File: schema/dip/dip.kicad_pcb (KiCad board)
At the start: 2 copper layers, 40.2 x 20.2 mm, 5 parts, among them J1 Conn_01x04_Male, J2 Conn_01x04_Male, SW1 SW_DIP_x04

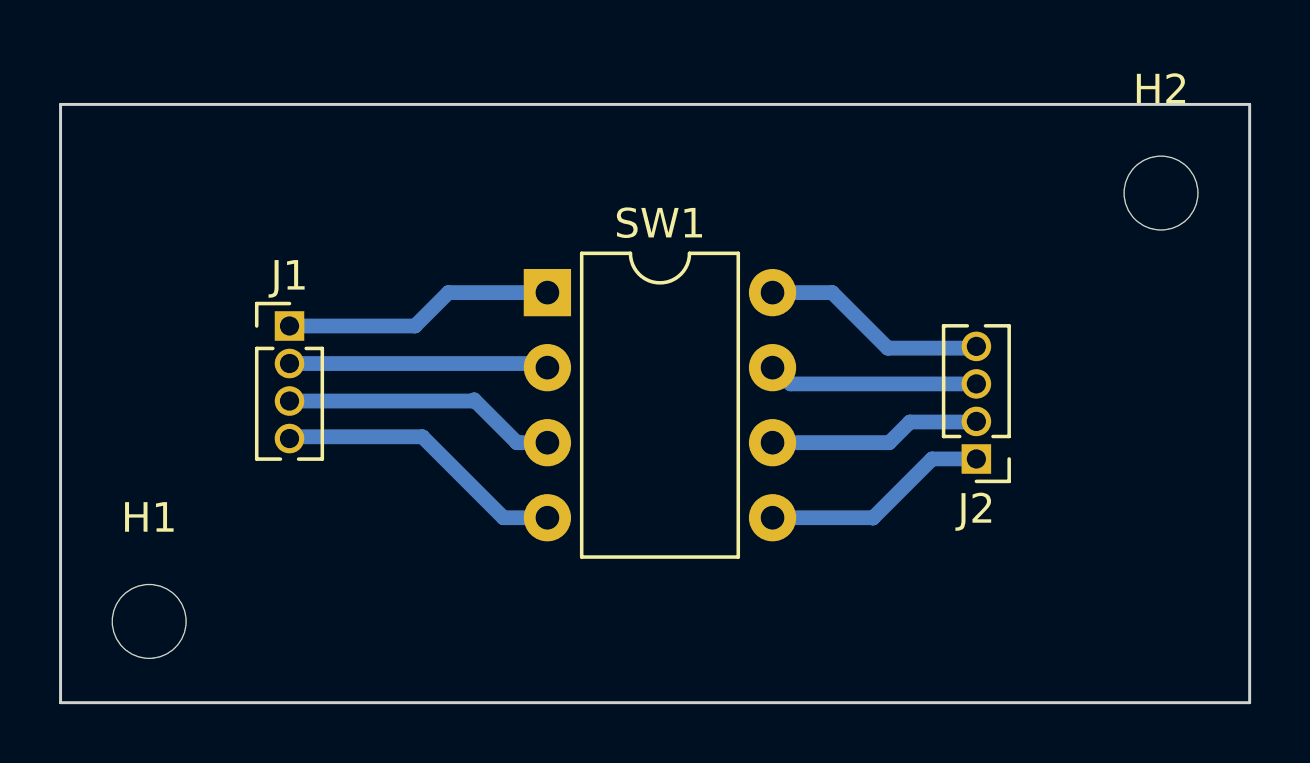
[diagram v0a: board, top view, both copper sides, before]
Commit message: support 02-silk directory
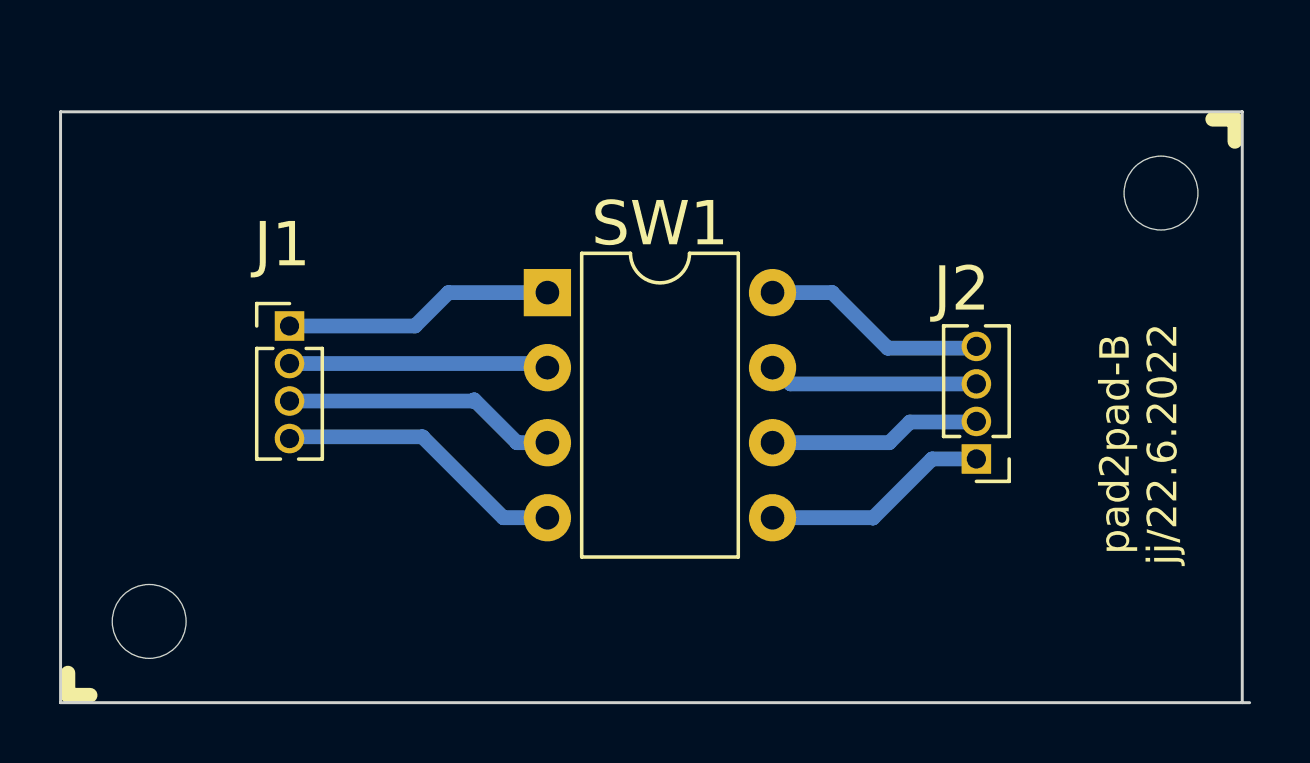
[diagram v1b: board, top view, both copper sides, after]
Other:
- board size 40.2 x 20.2 mm -> 40.2 x 20 mm
- board text added: "pad2pad-B jj/22.6.2022"

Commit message: alignment edges fixed
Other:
- board size 40.2 x 20 mm -> 40 x 20 mm

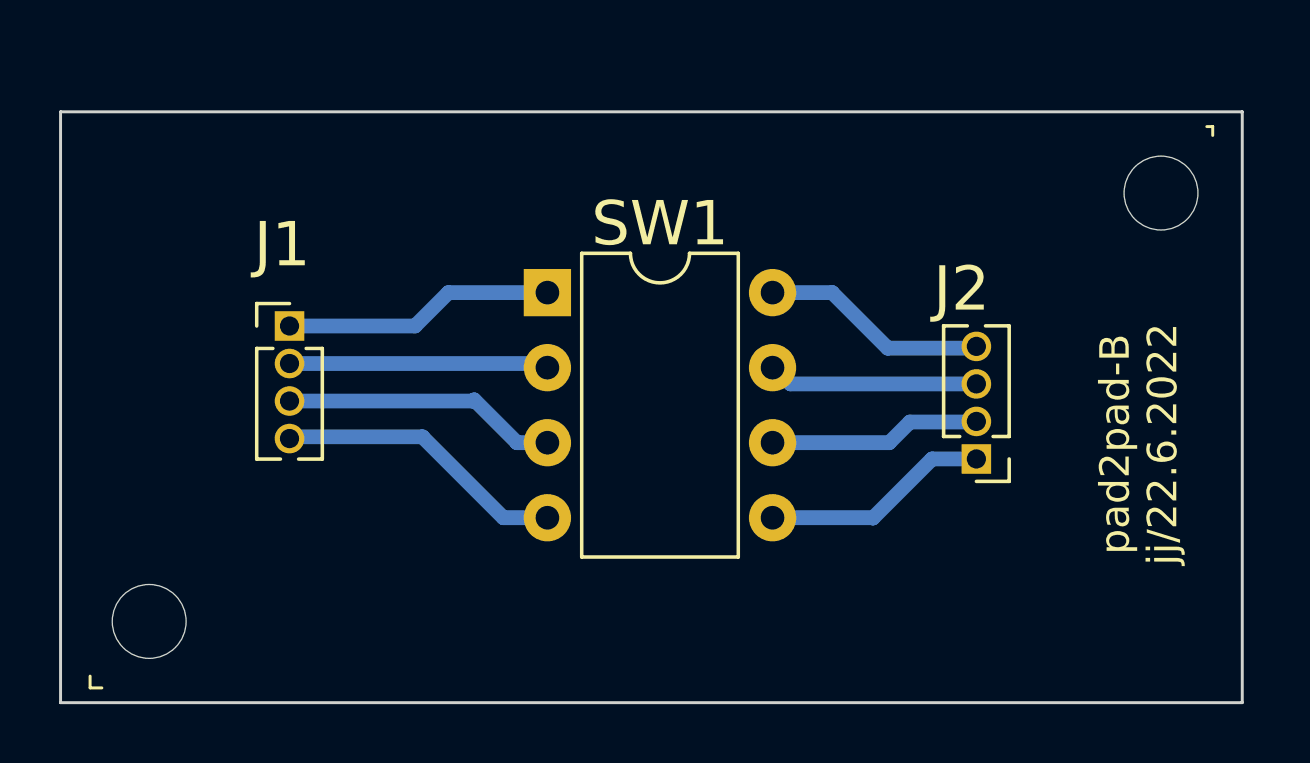
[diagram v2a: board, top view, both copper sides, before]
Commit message: fixed example: pad2pad, dip, added: milldrill option
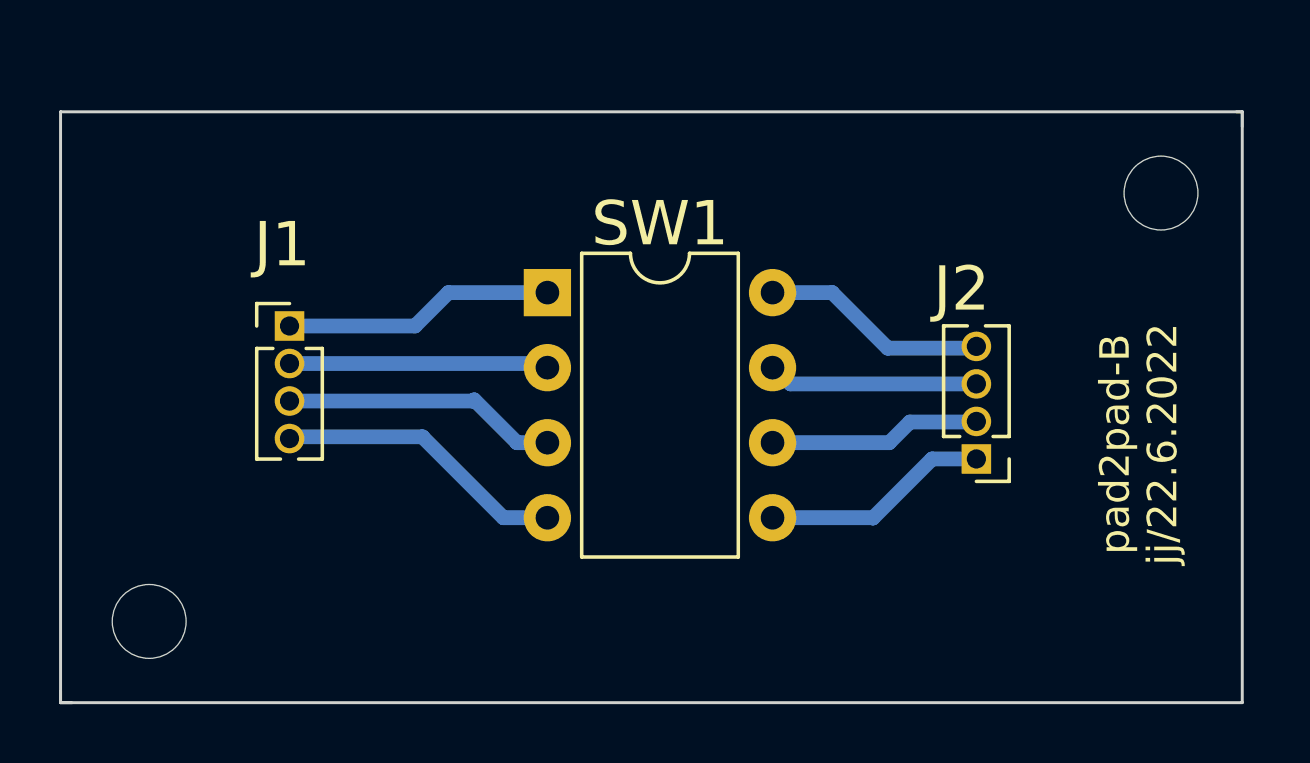
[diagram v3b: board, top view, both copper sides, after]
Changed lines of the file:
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@@
       (effects (font (size 1 1) (thickness 0.15)))
     )
+    (fp_circle (center 0 0) (end 2.5 0) (layer Cmts.User) (width 0.15))
     (fp_circle (center 0 0) (end 2.75 0) (layer F.CrtYd) (width 0.05))
-    (fp_circle (center 0 0) (end 2.5 0) (layer Cmts.User) (width 0.15))
     (fp_text user %R (at 0.3 0) (layer F.Fab)
       (effects (font (size 1 1) (thickness 0.15)))
@@
       (effects (font (size 1 1) (thickness 0.15)))
     )
+    (fp_circle (center 0 0) (end 2.5 0) (layer Cmts.User) (width 0.15))
     (fp_circle (center 0 0) (end 2.75 0) (layer F.CrtYd) (width 0.05))
-    (fp_circle (center 0 0) (end 2.5 0) (layer Cmts.User) (width 0.15))
     (fp_text user %R (at 0.3 0) (layer F.Fab)
       (effects (font (size 1 1) (thickness 0.15)))
@@
       (effects (font (size 1 1) (thickness 0.15)))
     )
+    (fp_line (start 1.635 -1.27) (end 6.985 -1.27) (layer F.Fab) (width 0.1))
+    (fp_line (start 6.985 -1.27) (end 6.985 8.89) (layer F.Fab) (width 0.1))
+    (fp_line (start 6.985 8.89) (end 0.635 8.89) (layer F.Fab) (width 0.1))
+    (fp_line (start 0.635 8.89) (end 0.635 -0.27) (layer F.Fab) (width 0.1))
+    (fp_line (start 0.635 -0.27) (end 1.635 -1.27) (layer F.Fab) (width 0.1))
+    (fp_line (start 2.81 -1.33) (end 1.16 -1.33) (layer F.SilkS) (width 0.12))
+    (fp_line (start 1.16 -1.33) (end 1.16 8.95) (layer F.SilkS) (width 0.12))
+    (fp_line (start 1.16 8.95) (end 6.46 8.95) (layer F.SilkS) (width 0.12))
+    (fp_line (start 6.46 8.95) (end 6.46 -1.33) (layer F.SilkS) (width 0.12))
+    (fp_line (start 6.46 -1.33) (end 4.81 -1.33) (layer F.SilkS) (width 0.12))
+    (fp_line (start -1.1 -1.55) (end -1.1 9.15) (layer F.CrtYd) (width 0.05))
+    (fp_line (start -1.1 9.15) (end 8.7 9.15) (layer F.CrtYd) (width 0.05))
+    (fp_line (start 8.7 9.15) (end 8.7 -1.55) (layer F.CrtYd) (width 0.05))
     (fp_line (start 8.7 -1.55) (end -1.1 -1.55) (layer F.CrtYd) (width 0.05))
-    (fp_line (start 8.7 9.15) (end 8.7 -1.55) (layer F.CrtYd) (width 0.05))
-    (fp_line (start -1.1 9.15) (end 8.7 9.15) (layer F.CrtYd) (width 0.05))
-    (fp_line (start -1.1 -1.55) (end -1.1 9.15) (layer F.CrtYd) (width 0.05))
-    (fp_line (start 6.46 -1.33) (end 4.81 -1.33) (layer F.SilkS) (width 0.12))
-    (fp_line (start 6.46 8.95) (end 6.46 -1.33) (layer F.SilkS) (width 0.12))
-    (fp_line (start 1.16 8.95) (end 6.46 8.95) (layer F.SilkS) (width 0.12))
-    (fp_line (start 1.16 -1.33) (end 1.16 8.95) (layer F.SilkS) (width 0.12))
-    (fp_line (start 2.81 -1.33) (end 1.16 -1.33) (layer F.SilkS) (width 0.12))
-    (fp_line (start 0.635 -0.27) (end 1.635 -1.27) (layer F.Fab) (width 0.1))
-    (fp_line (start 0.635 8.89) (end 0.635 -0.27) (layer F.Fab) (width 0.1))
-    (fp_line (start 6.985 8.89) (end 0.635 8.89) (layer F.Fab) (width 0.1))
-    (fp_line (start 6.985 -1.27) (end 6.985 8.89) (layer F.Fab) (width 0.1))
-    (fp_line (start 1.635 -1.27) (end 6.985 -1.27) (layer F.Fab) (width 0.1))
     (fp_text user %R (at 3.81 3.81) (layer F.Fab)
       (effects (font (size 1 1) (thickness 0.15)))
@@
       (effects (font (size 1 1) (thickness 0.15)))
     )
+    (fp_line (start -0.525 -0.635) (end 1.05 -0.635) (layer F.Fab) (width 0.1))
+    (fp_line (start 1.05 -0.635) (end 1.05 4.445) (layer F.Fab) (width 0.1))
+    (fp_line (start 1.05 4.445) (end -1.05 4.445) (layer F.Fab) (width 0.1))
+    (fp_line (start -1.05 4.445) (end -1.05 -0.11) (layer F.Fab) (width 0.1))
+    (fp_line (start -1.05 -0.11) (end -0.525 -0.635) (layer F.Fab) (width 0.1))
+    (fp_line (start -1.11 4.505) (end -0.30753 4.505) (layer F.SilkS) (width 0.12))
+    (fp_line (start 0.30753 4.505) (end 1.11 4.505) (layer F.SilkS) (width 0.12))
+    (fp_line (start -1.11 0.76) (end -1.11 4.505) (layer F.SilkS) (width 0.12))
+    (fp_line (start 1.11 0.76) (end 1.11 4.505) (layer F.SilkS) (width 0.12))
+    (fp_line (start -1.11 0.76) (end -0.563471 0.76) (layer F.SilkS) (width 0.12))
+    (fp_line (start 0.563471 0.76) (end 1.11 0.76) (layer F.SilkS) (width 0.12))
+    (fp_line (start -1.11 0) (end -1.11 -0.76) (layer F.SilkS) (width 0.12))
+    (fp_line (start -1.11 -0.76) (end 0 -0.76) (layer F.SilkS) (width 0.12))
+    (fp_line (start -1.55 -1.15) (end -1.55 4.95) (layer F.CrtYd) (width 0.05))
+    (fp_line (start -1.55 4.95) (end 1.55 4.95) (layer F.CrtYd) (width 0.05))
+    (fp_line (start 1.55 4.95) (end 1.55 -1.15) (layer F.CrtYd) (width 0.05))
     (fp_line (start 1.55 -1.15) (end -1.55 -1.15) (layer F.CrtYd) (width 0.05))
-    (fp_line (start 1.55 4.95) (end 1.55 -1.15) (layer F.CrtYd) (width 0.05))
-    (fp_line (start -1.55 4.95) (end 1.55 4.95) (layer F.CrtYd) (width 0.05))
-    (fp_line (start -1.55 -1.15) (end -1.55 4.95) (layer F.CrtYd) (width 0.05))
-    (fp_line (start -1.11 -0.76) (end 0 -0.76) (layer F.SilkS) (width 0.12))
-    (fp_line (start -1.11 0) (end -1.11 -0.76) (layer F.SilkS) (width 0.12))
-    (fp_line (start 0.563471 0.76) (end 1.11 0.76) (layer F.SilkS) (width 0.12))
-    (fp_line (start -1.11 0.76) (end -0.563471 0.76) (layer F.SilkS) (width 0.12))
-    (fp_line (start 1.11 0.76) (end 1.11 4.505) (layer F.SilkS) (width 0.12))
-    (fp_line (start -1.11 0.76) (end -1.11 4.505) (layer F.SilkS) (width 0.12))
-    (fp_line (start 0.30753 4.505) (end 1.11 4.505) (layer F.SilkS) (width 0.12))
-    (fp_line (start -1.11 4.505) (end -0.30753 4.505) (layer F.SilkS) (width 0.12))
-    (fp_line (start -1.05 -0.11) (end -0.525 -0.635) (layer F.Fab) (width 0.1))
-    (fp_line (start -1.05 4.445) (end -1.05 -0.11) (layer F.Fab) (width 0.1))
-    (fp_line (start 1.05 4.445) (end -1.05 4.445) (layer F.Fab) (width 0.1))
-    (fp_line (start 1.05 -0.635) (end 1.05 4.445) (layer F.Fab) (width 0.1))
-    (fp_line (start -0.525 -0.635) (end 1.05 -0.635) (layer F.Fab) (width 0.1))
     (fp_text user %R (at 0 1.905 90) (layer F.Fab)
       (effects (font (size 1 1) (thickness 0.15)))
@@
       (effects (font (size 1 1) (thickness 0.15)))
     )
+    (fp_line (start -0.525 -0.635) (end 1.05 -0.635) (layer F.Fab) (width 0.1))
+    (fp_line (start 1.05 -0.635) (end 1.05 4.445) (layer F.Fab) (width 0.1))
+    (fp_line (start 1.05 4.445) (end -1.05 4.445) (layer F.Fab) (width 0.1))
+    (fp_line (start -1.05 4.445) (end -1.05 -0.11) (layer F.Fab) (width 0.1))
+    (fp_line (start -1.05 -0.11) (end -0.525 -0.635) (layer F.Fab) (width 0.1))
+    (fp_line (start -1.11 4.505) (end -0.30753 4.505) (layer F.SilkS) (width 0.12))
+    (fp_line (start 0.30753 4.505) (end 1.11 4.505) (layer F.SilkS) (width 0.12))
+    (fp_line (start -1.11 0.76) (end -1.11 4.505) (layer F.SilkS) (width 0.12))
+    (fp_line (start 1.11 0.76) (end 1.11 4.505) (layer F.SilkS) (width 0.12))
+    (fp_line (start -1.11 0.76) (end -0.563471 0.76) (layer F.SilkS) (width 0.12))
+    (fp_line (start 0.563471 0.76) (end 1.11 0.76) (layer F.SilkS) (width 0.12))
+    (fp_line (start -1.11 0) (end -1.11 -0.76) (layer F.SilkS) (width 0.12))
+    (fp_line (start -1.11 -0.76) (end 0 -0.76) (layer F.SilkS) (width 0.12))
+    (fp_line (start -1.55 -1.15) (end -1.55 4.95) (layer F.CrtYd) (width 0.05))
+    (fp_line (start -1.55 4.95) (end 1.55 4.95) (layer F.CrtYd) (width 0.05))
+    (fp_line (start 1.55 4.95) (end 1.55 -1.15) (layer F.CrtYd) (width 0.05))
     (fp_line (start 1.55 -1.15) (end -1.55 -1.15) (layer F.CrtYd) (width 0.05))
-    (fp_line (start 1.55 4.95) (end 1.55 -1.15) (layer F.CrtYd) (width 0.05))
-    (fp_line (start -1.55 4.95) (end 1.55 4.95) (layer F.CrtYd) (width 0.05))
-    (fp_line (start -1.55 -1.15) (end -1.55 4.95) (layer F.CrtYd) (width 0.05))
-    (fp_line (start -1.11 -0.76) (end 0 -0.76) (layer F.SilkS) (width 0.12))
-    (fp_line (start -1.11 0) (end -1.11 -0.76) (layer F.SilkS) (width 0.12))
-    (fp_line (start 0.563471 0.76) (end 1.11 0.76) (layer F.SilkS) (width 0.12))
-    (fp_line (start -1.11 0.76) (end -0.563471 0.76) (layer F.SilkS) (width 0.12))
-    (fp_line (start 1.11 0.76) (end 1.11 4.505) (layer F.SilkS) (width 0.12))
-    (fp_line (start -1.11 0.76) (end -1.11 4.505) (layer F.SilkS) (width 0.12))
-    (fp_line (start 0.30753 4.505) (end 1.11 4.505) (layer F.SilkS) (width 0.12))
-    (fp_line (start -1.11 4.505) (end -0.30753 4.505) (layer F.SilkS) (width 0.12))
-    (fp_line (start -1.05 -0.11) (end -0.525 -0.635) (layer F.Fab) (width 0.1))
-    (fp_line (start -1.05 4.445) (end -1.05 -0.11) (layer F.Fab) (width 0.1))
-    (fp_line (start 1.05 4.445) (end -1.05 4.445) (layer F.Fab) (width 0.1))
-    (fp_line (start 1.05 -0.635) (end 1.05 4.445) (layer F.Fab) (width 0.1))
-    (fp_line (start -0.525 -0.635) (end 1.05 -0.635) (layer F.Fab) (width 0.1))
     (fp_text user %R (at 0 1.905 90) (layer F.Fab)
       (effects (font (size 1 1) (thickness 0.15)))
@@
     )
   )
-  (gr_line (start 1 -0.9) (end 1 -0.5) (layer F.SilkS) (width 0.1))
-  (gr_line (start 1 -0.5) (end 1.4 -0.5) (layer F.SilkS) (width 0.1))
-  (gr_line (start 38.8 -19.5) (end 39 -19.5) (layer F.SilkS) (width 0.1))
-  (gr_line (start 39 -19.5) (end 39 -19.2) (layer F.SilkS) (width 0.1))
+  (gr_line (start 0 -0.4) (end 0 0) (layer F.SilkS) (width 0.1))
+  (gr_line (start 0 0) (end 0.4 0) (layer F.SilkS) (width 0.1))
+  (gr_line (start 39.8 -20) (end 40 -20) (layer F.SilkS) (width 0.1))
+  (gr_line (start 40 -20) (end 40 -19.5) (layer F.SilkS) (width 0.1))
   (dimension 40 (width 0.15) (layer F.Fab)
     (gr_text "40,000 mm" (at 20 -24.3) (layer F.Fab)
